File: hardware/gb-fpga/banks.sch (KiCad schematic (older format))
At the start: 1 part, among them U1 xc7s25ftgb196

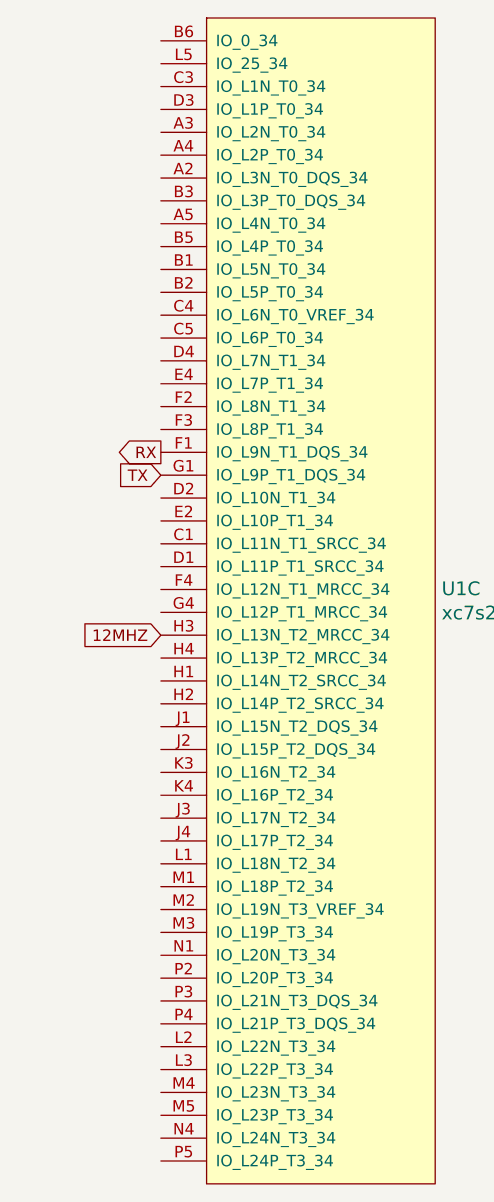
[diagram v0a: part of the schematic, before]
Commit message: Assign board connector pins to fpga
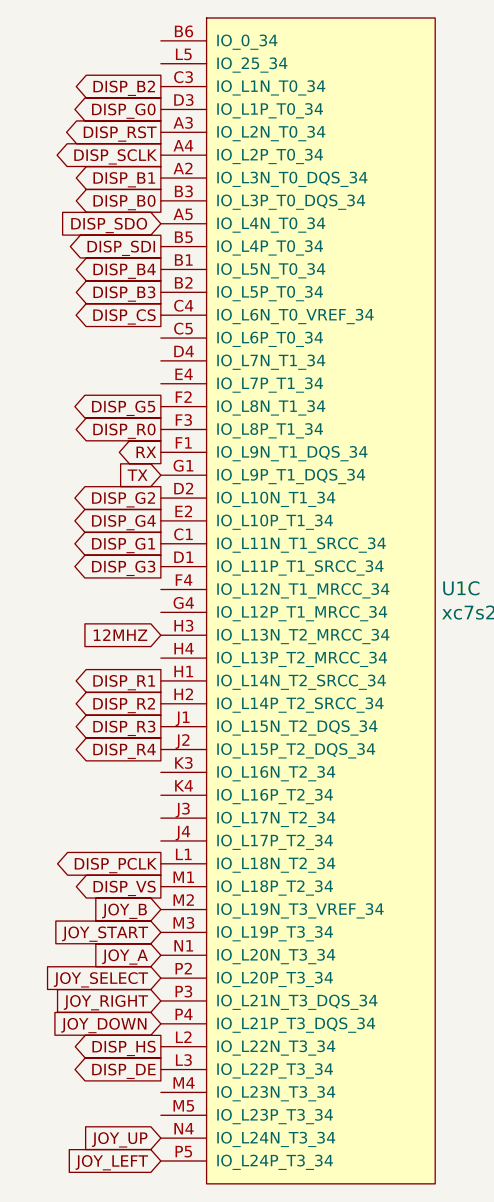
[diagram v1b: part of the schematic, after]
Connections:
- net DISP_B1: now reaches U1.A2 (IO_L3N_T0_DQS_34)
- net DISP_RST: now reaches U1.A3 (IO_L2N_T0_34)
- net DISP_SCLK: now reaches U1.A4 (IO_L2P_T0_34)
- net DISP_SDO: now reaches U1.A5 (IO_L4N_T0_34)
- net DISP_B4: now reaches U1.B1 (IO_L5N_T0_34)
- net DISP_B3: now reaches U1.B2 (IO_L5P_T0_34)
- net DISP_B0: now reaches U1.B3 (IO_L3P_T0_DQS_34)
- net DISP_SDI: now reaches U1.B5 (IO_L4P_T0_34)
- net DISP_G1: now reaches U1.C1 (IO_L11N_T1_SRCC_34)
- net DISP_B2: now reaches U1.C3 (IO_L1N_T0_34)
- net DISP_CS: now reaches U1.C4 (IO_L6N_T0_VREF_34)
- net DISP_G3: now reaches U1.D1 (IO_L11P_T1_SRCC_34)
- net DISP_G2: now reaches U1.D2 (IO_L10N_T1_34)
- net DISP_G0: now reaches U1.D3 (IO_L1P_T0_34)
- net DISP_G4: now reaches U1.E2 (IO_L10P_T1_34)
- net DISP_G5: now reaches U1.F2 (IO_L8N_T1_34)
- net DISP_R0: now reaches U1.F3 (IO_L8P_T1_34)
- net DISP_R1: now reaches U1.H1 (IO_L14N_T2_SRCC_34)
- net DISP_R2: now reaches U1.H2 (IO_L14P_T2_SRCC_34)
- net DISP_R3: now reaches U1.J1 (IO_L15N_T2_DQS_34)
- net DISP_R4: now reaches U1.J2 (IO_L15P_T2_DQS_34)
- net DISP_PCLK: now reaches U1.L1 (IO_L18N_T2_34)
- net DISP_HS: now reaches U1.L2 (IO_L22N_T3_34)
- net DISP_DE: now reaches U1.L3 (IO_L22P_T3_34)
- net DISP_VS: now reaches U1.M1 (IO_L18P_T2_34)
- net JOY_B: now reaches U1.M2 (IO_L19N_T3_VREF_34)
- net JOY_START: now reaches U1.M3 (IO_L19P_T3_34)
- net JOY_A: now reaches U1.N1 (IO_L20N_T3_34)
- net JOY_UP: now reaches U1.N4 (IO_L24N_T3_34)
- net JOY_SELECT: now reaches U1.P2 (IO_L20P_T3_34)
- net JOY_RIGHT: now reaches U1.P3 (IO_L21N_T3_DQS_34)
- net JOY_DOWN: now reaches U1.P4 (IO_L21P_T3_DQS_34)
- net JOY_LEFT: now reaches U1.P5 (IO_L24P_T3_34)
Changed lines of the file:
@@
 Text GLabel 6900 1850 0    50   BiDi ~ 0
 GB_D7
+Text GLabel 3300 2200 0    50   Input ~ 0
+DISP_SDO
+Text GLabel 3300 2300 0    50   Output ~ 0
+DISP_SDI
+Text GLabel 3300 1900 0    50   Output ~ 0
+DISP_SCLK
+Text GLabel 3300 2600 0    50   Output ~ 0
+DISP_CS
+Text GLabel 3300 1800 0    50   Output ~ 0
+DISP_RST
+Text GLabel 3300 2100 0    50   Output ~ 0
+DISP_B0
+Text GLabel 3300 2000 0    50   Output ~ 0
+DISP_B1
+Text GLabel 3300 1600 0    50   Output ~ 0
+DISP_B2
+Text GLabel 3300 2500 0    50   Output ~ 0
+DISP_B3
+Text GLabel 3300 2400 0    50   Output ~ 0
+DISP_B4
+Text GLabel 3300 1700 0    50   Output ~ 0
+DISP_G0
+Text GLabel 3300 3600 0    50   Output ~ 0
+DISP_G1
+Text GLabel 3300 3400 0    50   Output ~ 0
+DISP_G2
+Text GLabel 3300 3700 0    50   Output ~ 0
+DISP_G3
+Text GLabel 3300 3500 0    50   Output ~ 0
+DISP_G4
+Text GLabel 3300 3000 0    50   Output ~ 0
+DISP_G5
+Text GLabel 3300 3100 0    50   Output ~ 0
+DISP_R0
+Text GLabel 3300 4200 0    50   Output ~ 0
+DISP_R1
+Text GLabel 3300 4300 0    50   Output ~ 0
+DISP_R2
+Text GLabel 3300 4400 0    50   Output ~ 0
+DISP_R3
+Text GLabel 3300 4500 0    50   Output ~ 0
+DISP_R4
+Text GLabel 3300 5900 0    50   Output ~ 0
+DISP_DE
+Text GLabel 3300 5000 0    50   Output ~ 0
+DISP_PCLK
+Text GLabel 3300 5800 0    50   Output ~ 0
+DISP_HS
+Text GLabel 3300 5100 0    50   Output ~ 0
+DISP_VS
+Text GLabel 3300 5200 0    50   Input ~ 0
+JOY_B
+Text GLabel 3300 5400 0    50   Input ~ 0
+JOY_A
+Text GLabel 3300 5300 0    50   Input ~ 0
+JOY_START
+Text GLabel 3300 5500 0    50   Input ~ 0
+JOY_SELECT
+Text GLabel 3300 5600 0    50   Input ~ 0
+JOY_RIGHT
+Text GLabel 3300 6200 0    50   Input ~ 0
+JOY_UP
+Text GLabel 3300 5700 0    50   Input ~ 0
+JOY_DOWN
+Text GLabel 3300 6300 0    50   Input ~ 0
+JOY_LEFT
 $EndSCHEMATC

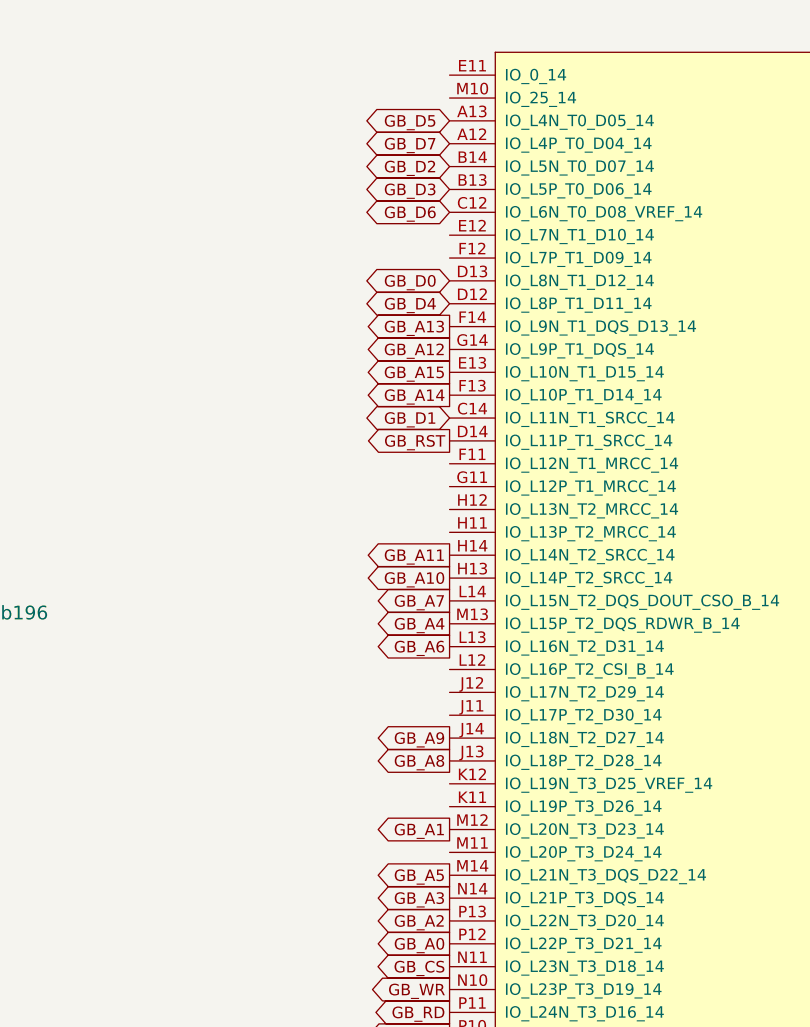
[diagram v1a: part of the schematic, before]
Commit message: Fan out the remaining pins
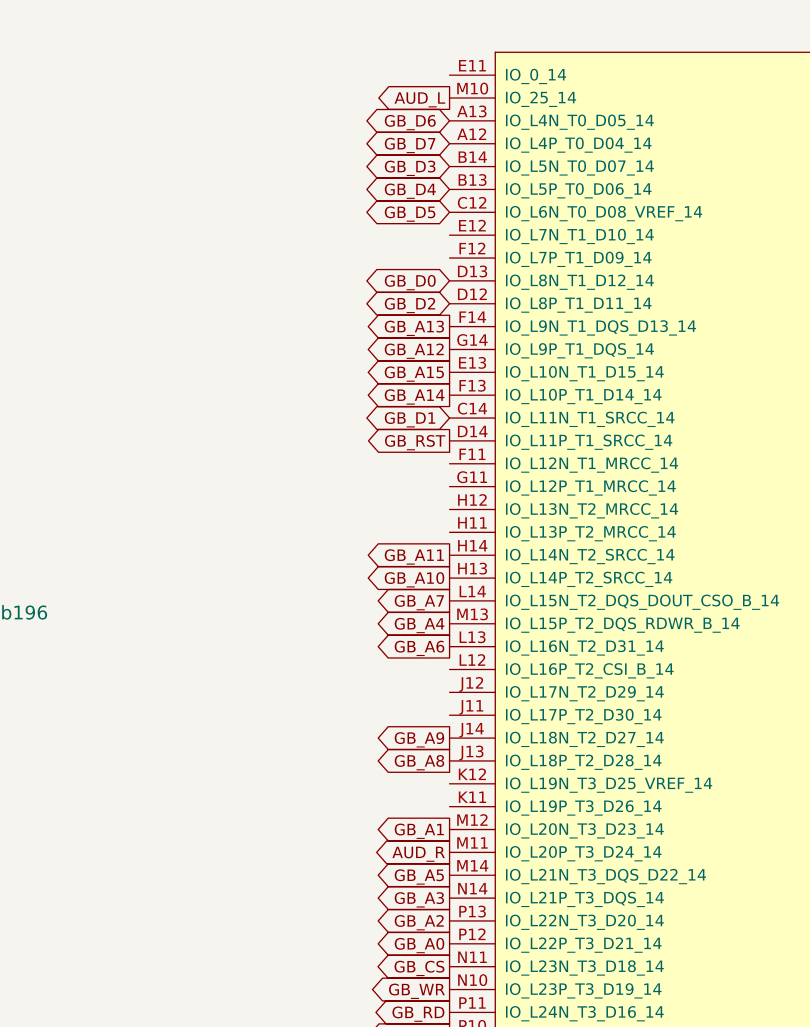
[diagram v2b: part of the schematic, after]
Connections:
- net GB_D2: now also U1.D12 (IO_L8P_T1_D11_14); no longer U1.B14 (IO_L5N_T0_D07_14)
- net GB_D3: now also U1.B14 (IO_L5N_T0_D07_14); no longer U1.B13 (IO_L5P_T0_D06_14)
- net GB_D4: now also U1.B13 (IO_L5P_T0_D06_14); no longer U1.D12 (IO_L8P_T1_D11_14)
- net GB_D5: now also U1.C12 (IO_L6N_T0_D08_VREF_14); no longer U1.A13 (IO_L4N_T0_D05_14)
- net GB_D6: now also U1.A13 (IO_L4N_T0_D05_14); no longer U1.C12 (IO_L6N_T0_D08_VREF_14)
- net AUD_L: now reaches U1.M10 (IO_25_14)
- net AUD_R: now reaches U1.M11 (IO_L20P_T3_D24_14)
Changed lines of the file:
@@
 Text GLabel 6900 3050 0    50   BiDi ~ 0
 GB_D1
+Text GLabel 6900 2550 0    50   BiDi ~ 0
+GB_D2
 Text GLabel 6900 1950 0    50   BiDi ~ 0
-GB_D2
+GB_D3
 Text GLabel 6900 2050 0    50   BiDi ~ 0
-GB_D3
-Text GLabel 6900 2550 0    50   BiDi ~ 0
 GB_D4
+Text GLabel 6900 2150 0    50   BiDi ~ 0
+GB_D5
 Text GLabel 6900 1750 0    50   BiDi ~ 0
-GB_D5
-Text GLabel 6900 2150 0    50   BiDi ~ 0
 GB_D6
 Text GLabel 6900 1850 0    50   BiDi ~ 0
@@
 Text GLabel 3300 6300 0    50   Input ~ 0
 JOY_LEFT
+Text GLabel 6900 1650 0    50   Output ~ 0
+AUD_L
+Text GLabel 6900 4950 0    50   Output ~ 0
+AUD_R
 $EndSCHEMATC

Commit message: Update bom
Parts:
- U1: Manufacturer Part Number (none) -> XC7S25-1FTGB196C
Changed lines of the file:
@@
 F 2 "" H 7100 1600 60  0001 L CNN
 F 3 "" H 7100 1400 60  0001 L CNN
+F 4 "XC7S25-1FTGB196C" H 6900 1550 50  0001 C CNN "Manufacturer Part Number"
 	2    6900 1550
 	1    0    0    -1
@@
 F 2 "" H 3500 1450 60  0001 L CNN
 F 3 "" H 3500 1250 60  0001 L CNN
+F 4 "XC7S25-1FTGB196C" H 3300 1400 50  0001 C CNN "Manufacturer Part Number"
 	3    3300 1400
 	1    0    0    -1
